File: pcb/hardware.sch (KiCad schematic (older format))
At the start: 7 parts, among them J1 Micro_SD_Card_Det_Hirose_DM3AT, U2 A33

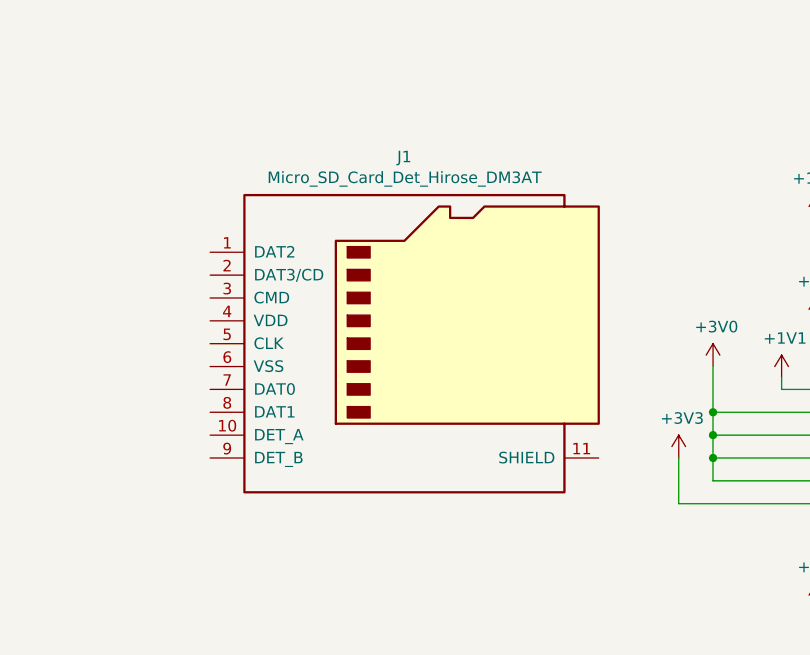
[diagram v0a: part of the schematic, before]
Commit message: Wired in the SD card
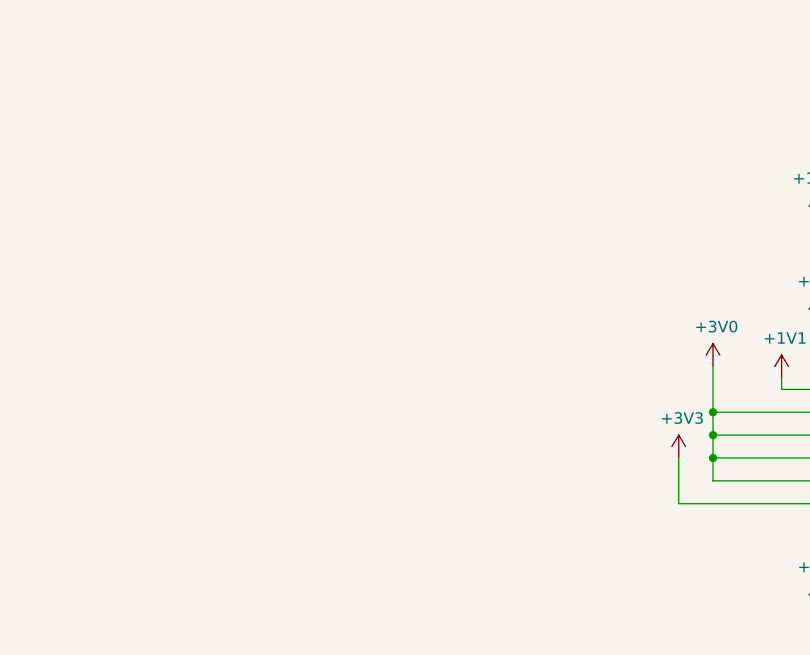
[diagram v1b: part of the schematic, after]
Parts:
- removed J1: Micro_SD_Card_Det_Hirose_DM3AT, Connector_Card:microSD_HC_Hirose_DM3AT-SF-PEJM5, symbol Connector:Micro_SD_Card_Det_Hirose_DM3AT
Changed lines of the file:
@@
-$EndComp
-$Comp
-L Device:R_Small_US R?
-U 1 1 607B18B8
-P 1200 1800
-AR Path="/60536DA4/607B18B8" Ref="R?"  Part="1"
-AR Path="/607B18B8" Ref="R5"  Part="1"
-F 0 "R5" H 1268 1846 50  0000 L CNN
-F 1 "1k" H 1268 1755 50  0000 L CNN
-F 2 "Resistor_SMD:R_0402_1005Metric" H 1200 1800 50  0001 C CNN
-F 3 "~" H 1200 1800 50  0001 C CNN
-	1    1200 1800
-	1    0    0    -1
 $EndComp
 $Comp
@@
 $EndSheet
 $Comp
-L Connector:Micro_SD_Card_Det_Hirose_DM3AT J1
-U 1 1 6062A02A
-P 6500 2400
-F 0 "J1" H 6450 3217 50  0000 C CNN
-F 1 "Micro_SD_Card_Det_Hirose_DM3AT" H 6450 3126 50  0000 C CNN
-F 2 "Connector_Card:microSD_HC_Hirose_DM3AT-SF-PEJM5" H 8550 3100 50  0001 C CNN
-F 3 "https://www.hirose.com/product/en/download_file/key_name/DM3/category/Catalog/doc_file_id/49662/?file_category_id=4&item_id=195&is_series=1" H 6500 2500 50  0001 C CNN
-	1    6500 2400
-	1    0    0    -1
-$EndComp
-$Comp
 L Allwinner_A33:A33 U2
 U 2 1 60BD8D67
@@
 Wire Bus Line
 	4050 1700 4050 3300
+$Comp
+L Device:R_Small_US R?
+U 1 1 607B18B8
+P 1200 1800
+AR Path="/60536DA4/607B18B8" Ref="R?"  Part="1"
+AR Path="/607B18B8" Ref="R5"  Part="1"
+F 0 "R5" H 1268 1846 50  0000 L CNN
+F 1 "1k" H 1268 1755 50  0000 L CNN
+F 2 "Resistor_SMD:R_0402_1005Metric" H 1200 1800 50  0001 C CNN
+F 3 "~" H 1200 1800 50  0001 C CNN
+	1    1200 1800
+	1    0    0    -1
+$EndComp
 $EndSCHEMATC

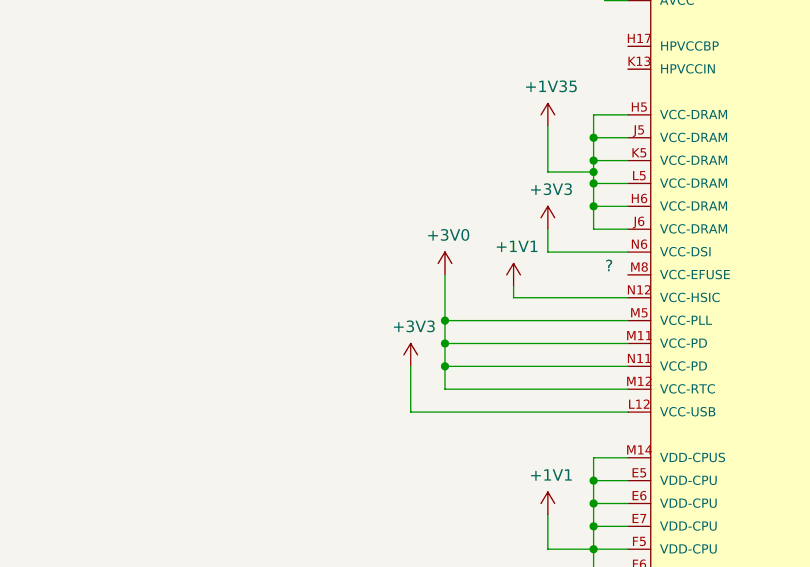
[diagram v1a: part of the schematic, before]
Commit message: Wired in the VCC-EFUSE stuff.
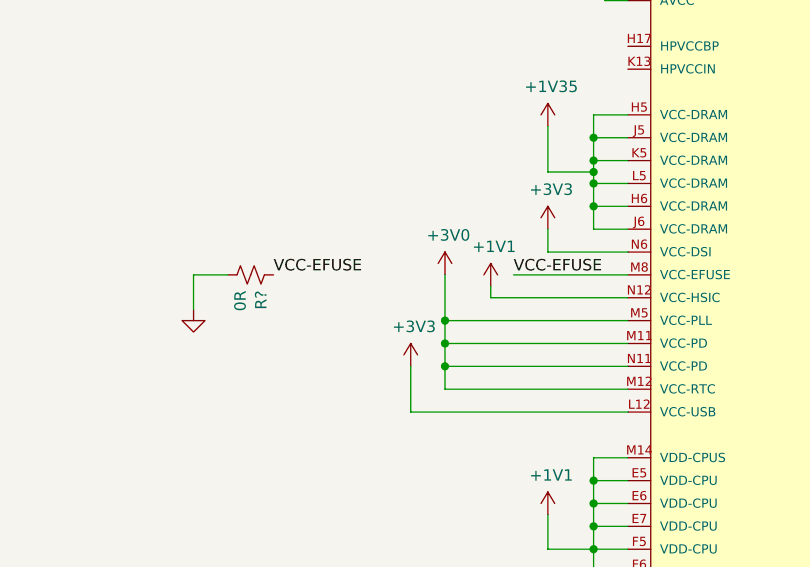
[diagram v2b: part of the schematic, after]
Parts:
- added R?: 0R, Resistor_SMD:R_0402_1005Metric, symbol Device:R_Small_US
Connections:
- net GND: now also R?.2
- net VCC-EFUSE: now reaches U2.M8 (VCC-EFUSE)
- net VCC-EFUSE: now also R?.1
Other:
- note removed: "?"
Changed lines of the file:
@@
 Wire Wire Line
 	7800 2800 7800 2700
-Text Notes 8500 2500 0    50   ~ 0
-?
 Wire Wire Line
 	8600 3300 8450 3300
 Wire Wire Line
-	8600 2600 8100 2600
+	8600 2600 8000 2600
 Wire Wire Line
 	7800 2700 7800 2500
 Wire Wire Line
-	8100 2600 8100 2550
+	8000 2600 8000 2550
 $Comp
 L power:+1V1 #PWR?
 U 1 1 60BD8E77
-P 8100 2550
+P 8000 2550
 AR Path="/60A30BFF/60BD8E77" Ref="#PWR?"  Part="1"
 AR Path="/60BD8E77" Ref="#PWR05"  Part="1"
-F 0 "#PWR05" H 8100 2400 50  0001 C CNN
-F 1 "+1V1" H 8115 2723 50  0000 C CNN
-F 2 "" H 8100 2550 50  0001 C CNN
-F 3 "" H 8100 2550 50  0001 C CNN
-	1    8100 2550
+F 0 "#PWR05" H 8000 2400 50  0001 C CNN
+F 1 "+1V1" H 8015 2723 50  0000 C CNN
+F 2 "" H 8000 2550 50  0001 C CNN
+F 3 "" H 8000 2550 50  0001 C CNN
+	1    8000 2550
 	1    0    0    -1
 $EndComp
@@
 Text Notes 2450 7050 0    50   ~ 0
 3v3 @ 1A. 75uS startup time.\n3v0 @ 1A. 75uS startup time.\n2v5 @ 300mA. 75uS startup time.\n1v35 @ 2A. 900uS startup time.\n1v1 @ 4A. 900uS startup time.
-Wire Bus Line
-	3950 3400 3950 3600
-Wire Bus Line
-	2150 1900 2150 3400
-Wire Bus Line
-	4050 1700 4050 3300
 $Comp
 L Device:R_Small_US R?
@@
 	1    0    0    -1
 $EndComp
+$Comp
+L Device:R_Small_US R?
+U 1 1 605E80D9
+P 6950 2500
+AR Path="/60536DA4/605E80D9" Ref="R?"  Part="1"
+AR Path="/605E80D9" Ref="R?"  Part="1"
+F 0 "R?" H 7018 2546 50  0000 L CNN
+F 1 "0R" H 7018 2455 50  0000 L CNN
+F 2 "Resistor_SMD:R_0402_1005Metric" H 6950 2500 50  0001 C CNN
+F 3 "~" H 6950 2500 50  0001 C CNN
+	1    6950 2500
+	0    1    1    0
+$EndComp
+Wire Wire Line
+	8600 2500 8100 2500
+Text Label 8100 2500 0    50   ~ 0
+VCC-EFUSE
+Text Label 7050 2500 0    50   ~ 0
+VCC-EFUSE
+$Comp
+L power:GND #PWR?
+U 1 1 60652B0A
+P 6700 2650
+AR Path="/60536DA4/60652B0A" Ref="#PWR?"  Part="1"
+AR Path="/60652B0A" Ref="#PWR?"  Part="1"
+AR Path="/60A30BFF/60652B0A" Ref="#PWR?"  Part="1"
+F 0 "#PWR?" H 6700 2400 50  0001 C CNN
+F 1 "GND" V 6705 2522 50  0001 R CNN
+F 2 "" H 6700 2650 50  0001 C CNN
+F 3 "" H 6700 2650 50  0001 C CNN
+	1    6700 2650
+	1    0    0    -1
+$EndComp
+Wire Wire Line
+	6700 2650 6700 2500
+Wire Wire Line
+	6700 2500 6850 2500
+Wire Bus Line
+	3950 3400 3950 3600
+Wire Bus Line
+	2150 1900 2150 3400
+Wire Bus Line
+	4050 1700 4050 3300
 $EndSCHEMATC

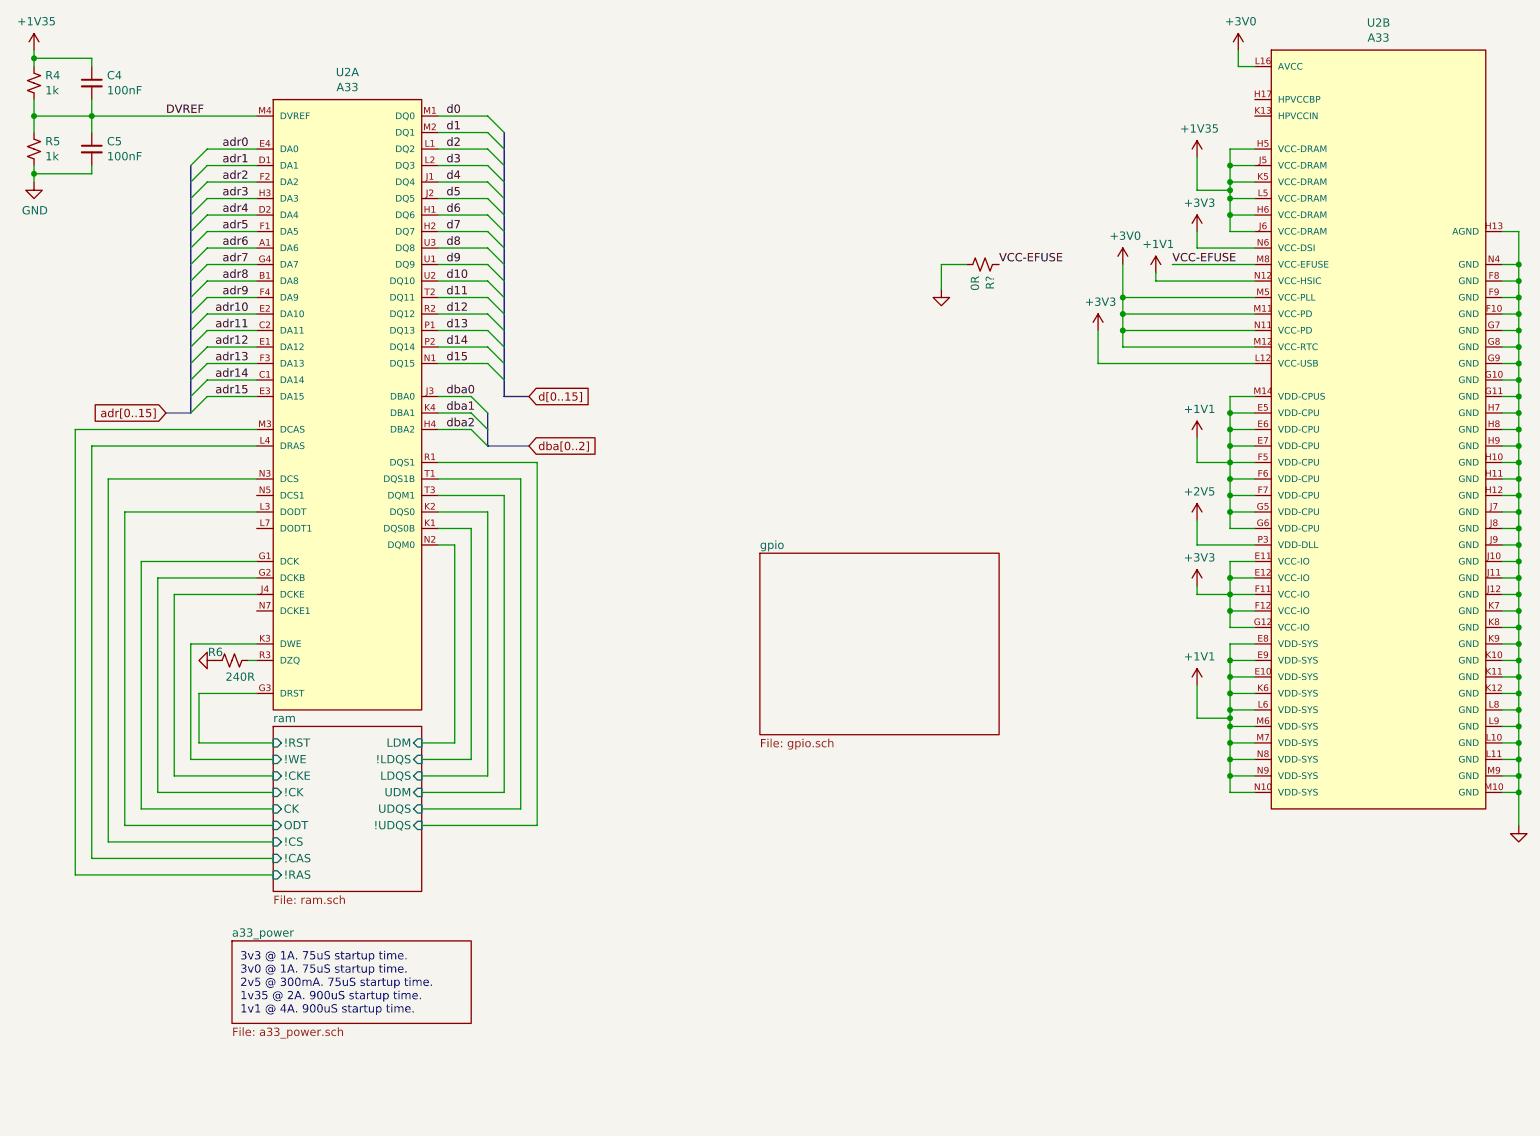
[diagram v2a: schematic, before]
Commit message: Decoupled the ram and A33
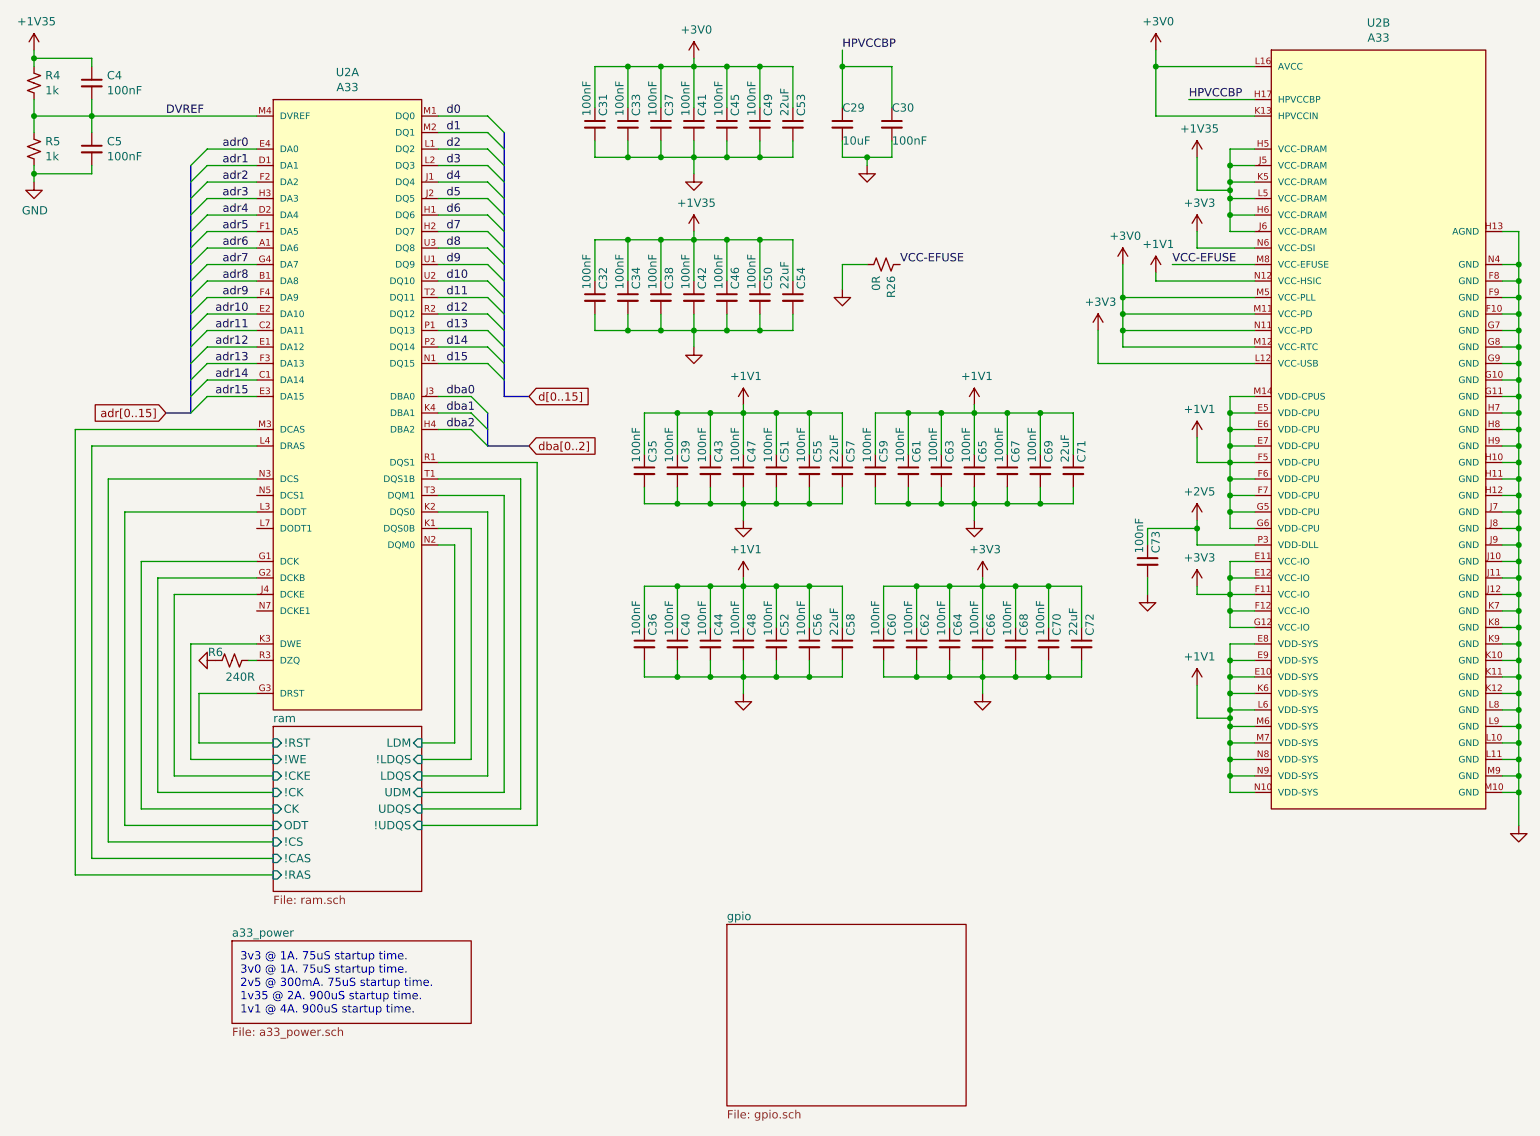
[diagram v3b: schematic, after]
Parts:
- added C29: 10uF, Capacitor_SMD:C_01005_0402Metric, symbol Device:C_Small
- added C30, C31, C32, C33, C34, C35, C36, C37, C38, C39, C40, C41, C42, C43, C44, C45, C46, C47, C48, C49, C50, C51, C52, C55, C56, C59, C60, C61, C62, C63, C64, C65, C66, C67, C68, C69, C70, C73: 100nF, Capacitor_SMD:C_01005_0402Metric, symbol Device:C_Small
- added C53, C54, C57, C58, C71, C72: 22uF, Capacitor_SMD:C_01005_0402Metric, symbol Device:C_Small
- gave numbers to parts that had none: 1
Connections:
- net +1V1: now also C35.1, C36.1, C39.1, C40.1, C43.1, C44.1, C47.1, C48.1, C51.1, C52.1, C55.1, C56.1, C57.1, C58.1, C59.1, C61.1, C63.1, C65.1, C67.1, C69.1, C71.1
- net +1V35: now also C32.1, C34.1, C38.1, C42.1, C46.1, C50.1, C54.1
- net +2V5: now also C73.1
- net +3V0: now also U2.K13 (HPVCCIN), C31.1, C33.1, C37.1, C41.1, C45.1, C49.1, C53.1
- net +3V3: now also C60.1, C62.1, C64.1, C66.1, C68.1, C70.1, C72.1
- net GND: now also C29.2, C30.2, C31.2, C32.2, C33.2, C34.2, C35.2, C36.2, C37.2, C38.2, C39.2, C40.2, C41.2, C42.2, C43.2, C44.2, C45.2, C46.2, C47.2, C48.2, C49.2, C50.2, C51.2, C52.2, C53.2, C54.2, C55.2, C56.2, C57.2, C58.2, C59.2, C60.2, C61.2, C62.2, C63.2, C64.2, C65.2, C66.2, C67.2, C68.2, C69.2, C70.2, C71.2, C72.2, C73.2
- net HPVCCBP: now reaches U2.H17 (HPVCCBP)
- net HPVCCBP: now also C29.1, C30.1
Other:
- moved on the sheet: R26

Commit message: Figured out all the crystals
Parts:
- added R27, R28: 0R, Resistor_SMD:R_0402_1005Metric, symbol Device:R_Small_US
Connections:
- net ram/!CK: now also R28.2; no longer U2.G2 (DCKB)
- net ram/CK: now also R27.2; no longer U2.G1 (DCK)
- new net: R27.1, U2.G1 (DCK)
- new net: R28.1, U2.G2 (DCKB)
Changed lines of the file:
@@
 	2050 4500 2050 5600
 Wire Wire Line
-	2550 4400 1950 4400
+	2550 4400 2300 4400
 Wire Wire Line
 	1950 4400 1950 5700
 Wire Wire Line
-	2550 4300 1850 4300
+	2550 4300 2300 4300
 Wire Wire Line
 	1850 4300 1850 5800
@@
 Wire Bus Line
 	4050 1700 4050 3300
+$Comp
+L Device:R_Small_US R?
+U 1 1 606E3432
+P 2200 4300
+AR Path="/60536DA4/606E3432" Ref="R?"  Part="1"
+AR Path="/606E3432" Ref="R27"  Part="1"
+F 0 "R27" V 2150 4400 50  0000 L CNN
+F 1 "0R" V 2150 4100 50  0000 L CNN
+F 2 "Resistor_SMD:R_0402_1005Metric" H 2200 4300 50  0001 C CNN
+F 3 "~" H 2200 4300 50  0001 C CNN
+	1    2200 4300
+	0    1    1    0
+$EndComp
+Wire Wire Line
+	2100 4300 1850 4300
+$Comp
+L Device:R_Small_US R?
+U 1 1 606E81AC
+P 2200 4400
+AR Path="/60536DA4/606E81AC" Ref="R?"  Part="1"
+AR Path="/606E81AC" Ref="R28"  Part="1"
+F 0 "R28" V 2150 4500 50  0000 L CNN
+F 1 "0R" V 2150 4200 50  0000 L CNN
+F 2 "Resistor_SMD:R_0402_1005Metric" H 2200 4400 50  0001 C CNN
+F 3 "~" H 2200 4400 50  0001 C CNN
+	1    2200 4400
+	0    1    1    0
+$EndComp
+Wire Wire Line
+	2100 4400 1950 4400
 $EndSCHEMATC

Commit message: Backing up
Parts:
- C29, C30, C31, C32, C33, C34, C35, C36, C37, C38, C39, C4, C40, C41, C42, C43, C44, C45, C46, C47, C48, C49, C5, C50, C51, C52, C53, C54, C55, C56, C57, C58, C59, C60, C61, C62, C63, C64, C65, C66, C67, C68, C69, C70, C71, C72, C73: footprint Capacitor_SMD:C_01005_0402Metric -> Capacitor_SMD:C_0402_1005Metric
- R27, R28: value 0R -> 22R

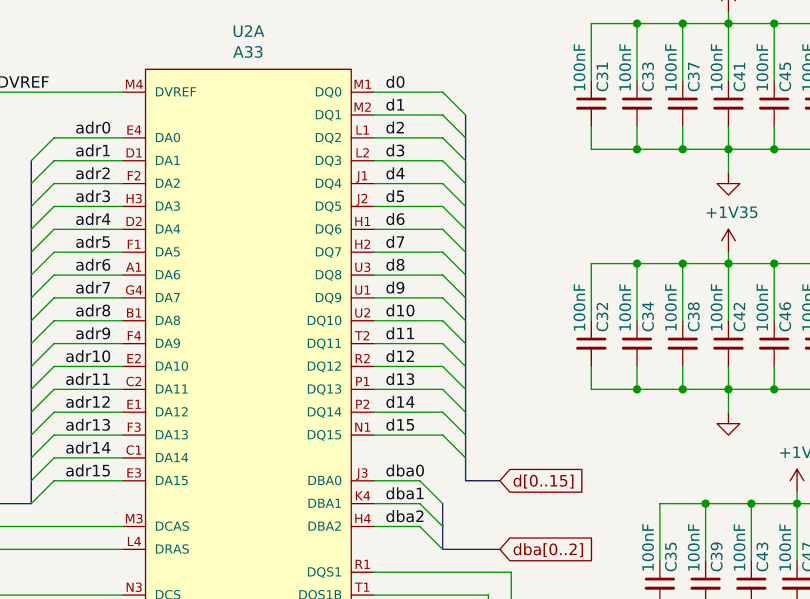
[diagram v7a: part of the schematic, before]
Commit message: RAM hooked up
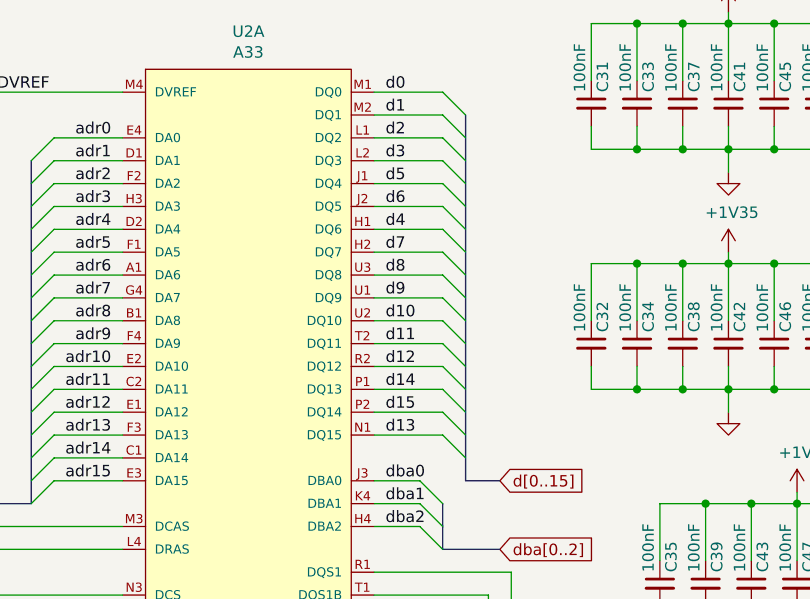
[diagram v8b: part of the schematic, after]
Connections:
- net d13: now also U2.N1 (DQ15); no longer U2.P1 (DQ13)
- net d14: now also U2.P1 (DQ13); no longer U2.P2 (DQ14)
- net d15: now also U2.P2 (DQ14); no longer U2.N1 (DQ15)
- net d4: now also U2.H1 (DQ6); no longer U2.J1 (DQ4)
- net d5: now also U2.J1 (DQ4); no longer U2.J2 (DQ5)
- net d6: now also U2.J2 (DQ5); no longer U2.H1 (DQ6)
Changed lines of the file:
@@
 Text Label 3700 1900 0    50   ~ 0
 d3
+Text Label 3700 2200 0    50   ~ 0
+d4
 Text Label 3700 2000 0    50   ~ 0
-d4
+d5
 Text Label 3700 2100 0    50   ~ 0
-d5
-Text Label 3700 2200 0    50   ~ 0
 d6
 Text Label 3700 2300 0    50   ~ 0
@@
 Text Label 3700 2800 0    50   ~ 0
 d12
+Text Label 3700 3100 0    50   ~ 0
+d13
 Text Label 3700 2900 0    50   ~ 0
-d13
+d14
 Text Label 3700 3000 0    50   ~ 0
-d14
-Text Label 3700 3100 0    50   ~ 0
 d15
 Wire Bus Line
@@
 Wire Wire Line
 	2550 4300 2300 4300
-Wire Bus Line
-	3950 3400 3950 3600
-Wire Bus Line
-	2150 1900 2150 3400
-Wire Bus Line
-	4050 1700 4050 3300
 $Comp
 L Device:R_Small_US R?
@@
 	0    1    1    0
 $EndComp
+Wire Bus Line
+	3950 3400 3950 3600
+Wire Bus Line
+	2150 1900 2150 3400
+Wire Bus Line
+	4050 1700 4050 3300
 $EndSCHEMATC
